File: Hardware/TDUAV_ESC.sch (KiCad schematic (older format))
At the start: 72 parts, among them J1 USB_B_Micro, J2 PWM-UBEC, J3 UART, J4 CH340, J5 BATT, J6 GND, J7 PHASE_A, J8 PHASE_B, J9 PHASE_C, Q1 IRLZ44NS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

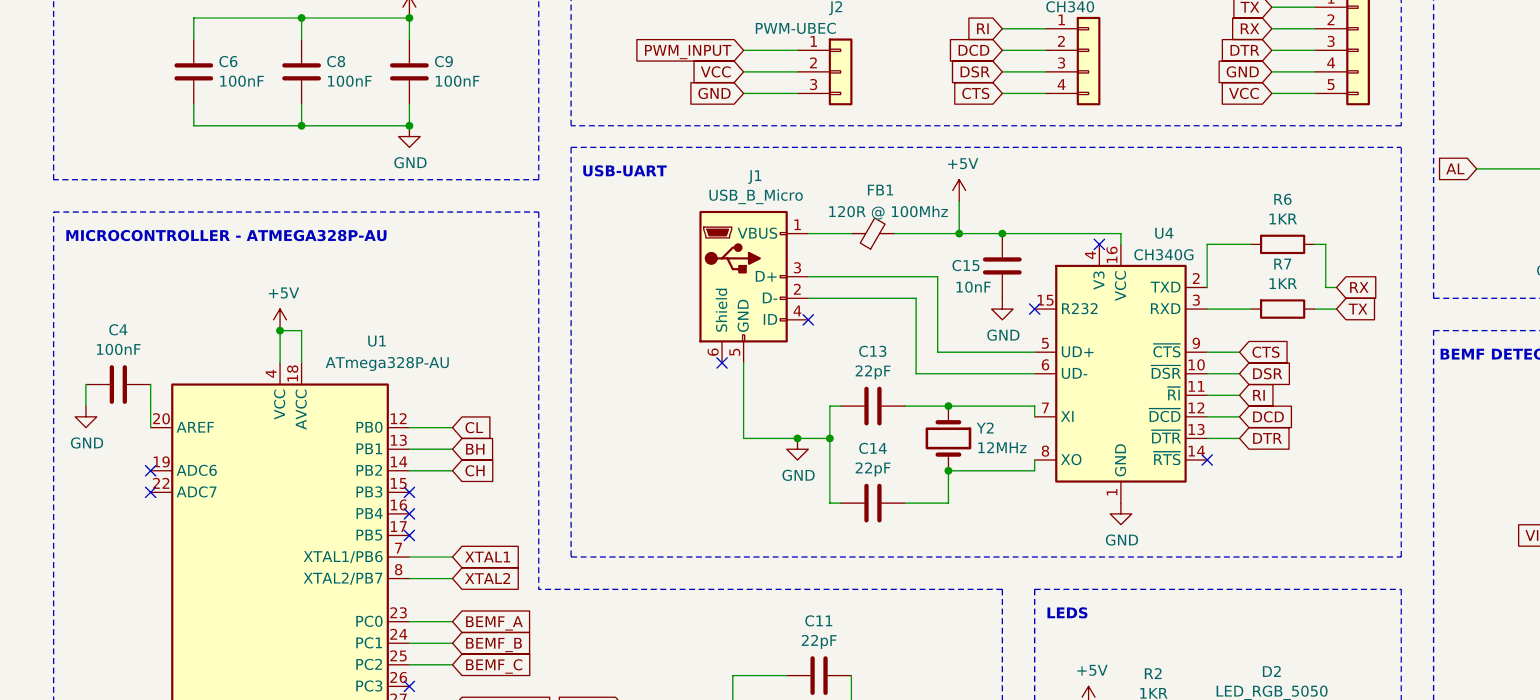
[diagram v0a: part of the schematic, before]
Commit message: Added cap to ch340 and changed values of decoupling caps
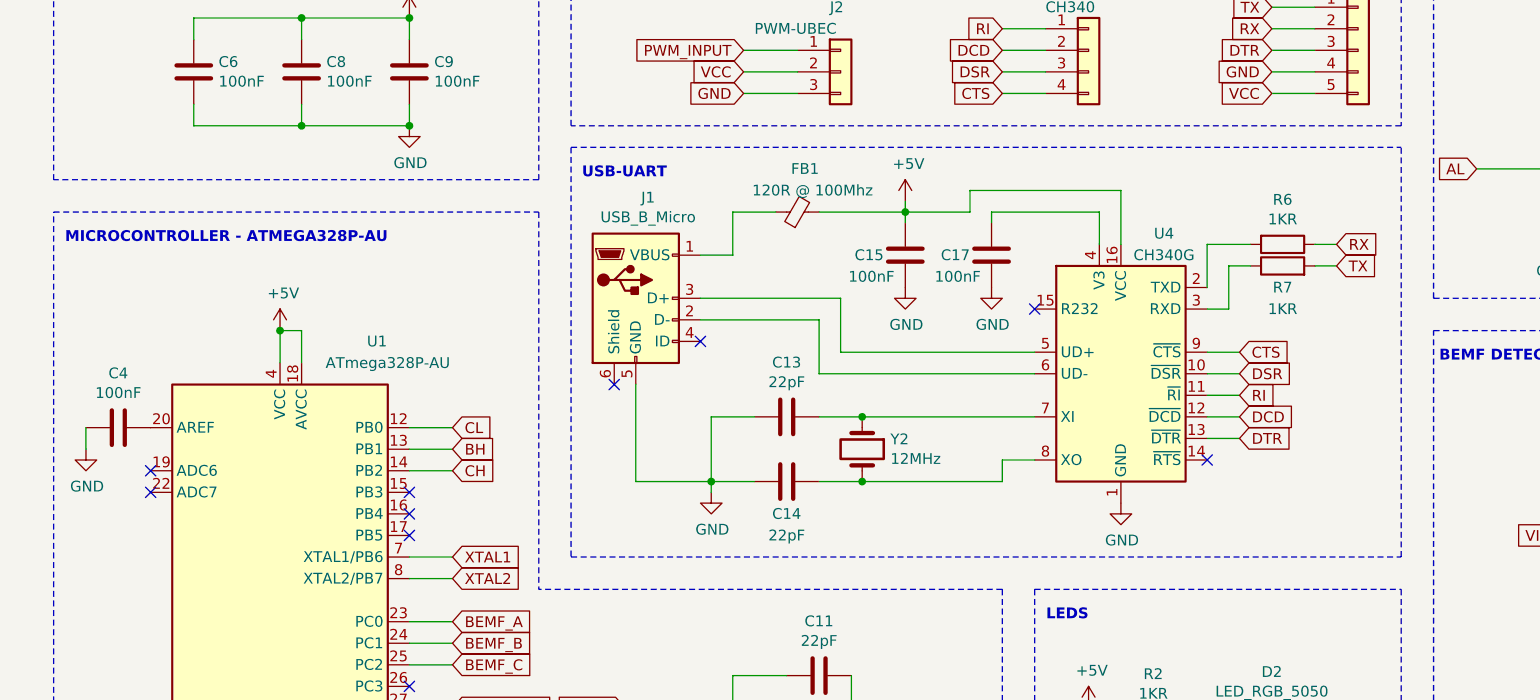
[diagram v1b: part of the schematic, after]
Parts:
- added C17: 100nF, Capacitor_SMD:C_1206_3216Metric_Pad1.33x1.80mm_HandSolder, symbol Device:C
- C15: value 10nF -> 100nF
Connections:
- net GND: now also C17.1
- net TX: now also R7.2; no longer R7.1
- net at U4.3 (RXD): now also R7.1; no longer R7.2
- net at U4.4 (V3): now also C17.2
- no-connect marks 17 -> 16
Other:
- moved on the sheet: C13, C14, C15, C4, FB1, J1, R7, Y2
